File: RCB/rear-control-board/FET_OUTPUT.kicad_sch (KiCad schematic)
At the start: 3 parts, among them Q3 STB15N80K5, Q4 STB15N80K5, Q5 STB15N80K5

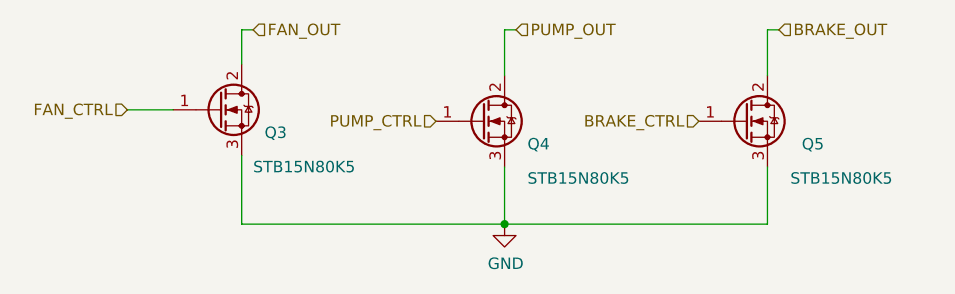
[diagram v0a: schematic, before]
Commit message: working on layout
Updating traces for RCB and organizing HVB
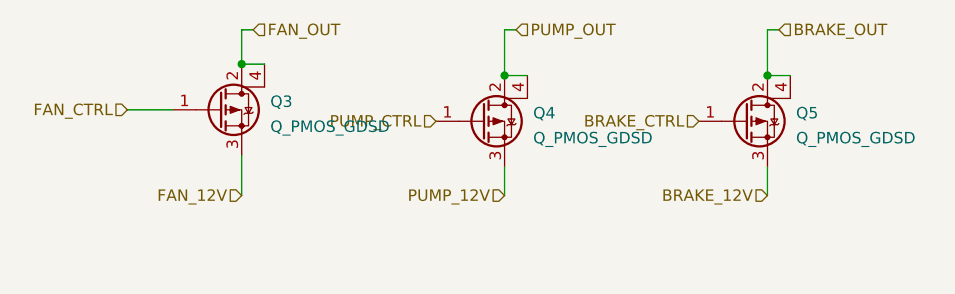
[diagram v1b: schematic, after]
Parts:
- removed Q3, Q4, Q5: STB15N80K5, Package_TO_SOT_SMD:TO-263-2, symbol Transistor_FET:STB15N80K5
- added Q3, Q4, Q5: Q_PMOS_GDSD, Package_TO_SOT_SMD:TO-252-3_TabPin4, symbol Device:Q_PMOS_GDSD
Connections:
- net BRAKE_CTRL: now also Q5.1 (G)
- net BRAKE_OUT: now also Q5.2 (D), Q5.4 (D)
- net FAN_CTRL: now also Q3.1 (G)
- net FAN_OUT: now also Q3.2 (D), Q3.4 (D)
- net PUMP_CTRL: now also Q4.1 (G)
- net PUMP_OUT: now also Q4.2 (D), Q4.4 (D)
- new net BRAKE_12V: Q5.3 (S)
- new net FAN_12V: Q3.3 (S)
- new net PUMP_12V: Q4.3 (S)
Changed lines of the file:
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@@
 (kicad_sch (version 20211123) (generator eeschema)
   (paper "A4")
-  (junction (at 87.63 81.28) (diameter 0) (color 0 0 0 0)
+  (junction (at 87.63 64.77) (diameter 0) (color 0 0 0 0)
   )
-  (wire (pts (xy 58.42 81.28) (xy 87.63 81.28))
+  (junction (at 116.84 64.77) (diameter 0) (color 0 0 0 0)
+  )
+  (junction (at 58.42 63.5) (diameter 0) (color 0 0 0 0)
+  )
+  (wire (pts (xy 87.63 64.77) (xy 90.17 64.77))
     (stroke (width 0) (type default) (color 0 0 0 0))
   )
-  (wire (pts (xy 87.63 81.28) (xy 87.63 74.93))
+  (wire (pts (xy 58.42 73.66) (xy 58.42 78.105))
     (stroke (width 0) (type default) (color 0 0 0 0))
   )
@@
     (stroke (width 0) (type default) (color 0 0 0 0))
   )
+  (wire (pts (xy 58.42 63.5) (xy 60.96 63.5))
+    (stroke (width 0) (type default) (color 0 0 0 0))
+  )
+  (wire (pts (xy 87.63 74.93) (xy 87.63 78.105))
+    (stroke (width 0) (type default) (color 0 0 0 0))
+  )
+  (wire (pts (xy 116.84 64.77) (xy 119.38 64.77))
+    (stroke (width 0) (type default) (color 0 0 0 0))
+  )
   (wire (pts (xy 87.63 59.69) (xy 87.63 64.77))
     (stroke (width 0) (type default) (color 0 0 0 0))
   )
   (wire (pts (xy 59.69 59.69) (xy 58.42 59.69))
-    (stroke (width 0) (type default) (color 0 0 0 0))
-  )
-  (wire (pts (xy 58.42 73.66) (xy 58.42 81.28))
     (stroke (width 0) (type default) (color 0 0 0 0))
   )
@@
     (stroke (width 0) (type default) (color 0 0 0 0))
   )
-  (wire (pts (xy 116.84 74.93) (xy 116.84 81.28))
+  (wire (pts (xy 45.72 68.58) (xy 50.8 68.58))
     (stroke (width 0) (type default) (color 0 0 0 0))
   )
-  (wire (pts (xy 116.84 81.28) (xy 87.63 81.28))
+  (wire (pts (xy 116.84 74.93) (xy 116.84 78.105))
     (stroke (width 0) (type default) (color 0 0 0 0))
   )
-  (wire (pts (xy 45.72 68.58) (xy 50.8 68.58))
-    (stroke (width 0) (type default) (color 0 0 0 0))
+  (hierarchical_label "FAN_12V" (shape input) (at 58.42 78.105 180)
+    (effects (font (size 1.27 1.27)) (justify right))
+  )
+  (hierarchical_label "PUMP_12V" (shape input) (at 87.63 78.105 180)
+    (effects (font (size 1.27 1.27)) (justify right))
   )
   (hierarchical_label "PUMP_CTRL" (shape input) (at 80.01 69.85 180)
@@
   )
   (hierarchical_label "FAN_CTRL" (shape input) (at 45.72 68.58 180)
+    (effects (font (size 1.27 1.27)) (justify right))
+  )
+  (hierarchical_label "BRAKE_12V" (shape input) (at 116.84 78.105 180)
     (effects (font (size 1.27 1.27)) (justify right))
   )
@@
     (effects (font (size 1.27 1.27)) (justify right))
   )
-  (symbol (lib_id "Transistor_FET:STB15N80K5") (at 55.88 68.58 0) (unit 1)
-    (in_bom yes) (on_board yes)
-    (property "Reference" "Q3" (id 0) (at 60.96 71.12 0)
+  (symbol (lib_id "Device:Q_PMOS_GDSD") (at 114.3 69.85 0) (unit 1)
+    (in_bom yes) (on_board yes) (fields_autoplaced)
+    (property "Reference" "Q5" (id 0) (at 120.015 68.9415 0)
       (effects (font (size 1.27 1.27)) (justify left))
     )
-    (property "Value" "STB15N80K5" (id 1) (at 59.69 74.93 0)
+    (property "Value" "Q_PMOS_GDSD" (id 1) (at 120.015 71.7166 0)
       (effects (font (size 1.27 1.27)) (justify left))
     )
-    (property "Footprint" "Package_TO_SOT_SMD:TO-263-2" (id 2) (at 60.96 70.485 0)
-      (effects (font (size 1.27 1.27) italic) (justify left) hide)
+    (property "Footprint" "Package_TO_SOT_SMD:TO-252-3_TabPin4" (id 2) (at 119.38 67.31 0)
+      (effects (font (size 1.27 1.27)) hide)
     )
-    (property "Datasheet" "https://www.st.com/resource/en/datasheet/stb15n80k5.pdf" (id 3) (at 55.88 68.58 0)
-      (effects (font (size 1.27 1.27)) (justify left) hide)
+    (property "Datasheet" "~" (id 3) (at 114.3 69.85 0)
+      (effects (font (size 1.27 1.27)) hide)
     )
     (pin "1")
     (pin "2")
     (pin "3")
+    (pin "4")
   )
-  (symbol (lib_id "power:GND") (at 87.63 81.28 0) (unit 1)
-    (in_bom yes) (on_board yes)
-    (property "Reference" "#PWR0121" (id 0) (at 87.63 87.63 0)
+  (symbol (lib_id "Device:Q_PMOS_GDSD") (at 85.09 69.85 0) (unit 1)
+    (in_bom yes) (on_board yes) (fields_autoplaced)
+    (property "Reference" "Q4" (id 0) (at 90.805 68.9415 0)
+      (effects (font (size 1.27 1.27)) (justify left))
+    )
+    (property "Value" "Q_PMOS_GDSD" (id 1) (at 90.805 71.7166 0)
+      (effects (font (size 1.27 1.27)) (justify left))
+    )
+    (property "Footprint" "Package_TO_SOT_SMD:TO-252-3_TabPin4" (id 2) (at 90.17 67.31 0)
       (effects (font (size 1.27 1.27)) hide)
     )
-    (property "Value" "GND" (id 1) (at 87.757 85.6742 0))
-    (property "Footprint" "" (id 2) (at 87.63 81.28 0)
+    (property "Datasheet" "~" (id 3) (at 85.09 69.85 0)
       (effects (font (size 1.27 1.27)) hide)
-    )
-    (property "Datasheet" "" (id 3) (at 87.63 81.28 0)
-      (effects (font (size 1.27 1.27)) hide)
-    )
-    (pin "1")
-  )
-  (symbol (lib_id "Transistor_FET:STB15N80K5") (at 85.09 69.85 0) (unit 1)
-    (in_bom yes) (on_board yes)
-    (property "Reference" "Q4" (id 0) (at 90.17 72.39 0)
-      (effects (font (size 1.27 1.27)) (justify left))
-    )
-    (property "Value" "STB15N80K5" (id 1) (at 90.17 76.2 0)
-      (effects (font (size 1.27 1.27)) (justify left))
-    )
-    (property "Footprint" "Package_TO_SOT_SMD:TO-263-2" (id 2) (at 90.17 71.755 0)
-      (effects (font (size 1.27 1.27) italic) (justify left) hide)
-    )
-    (property "Datasheet" "https://www.st.com/resource/en/datasheet/stb15n80k5.pdf" (id 3) (at 85.09 69.85 0)
-      (effects (font (size 1.27 1.27)) (justify left) hide)
     )
     (pin "1")
     (pin "2")
     (pin "3")
+    (pin "4")
   )
-  (symbol (lib_id "Transistor_FET:STB15N80K5") (at 114.3 69.85 0) (unit 1)
-    (in_bom yes) (on_board yes)
-    (property "Reference" "Q5" (id 0) (at 120.65 72.39 0)
+  (symbol (lib_id "Device:Q_PMOS_GDSD") (at 55.88 68.58 0) (unit 1)
+    (in_bom yes) (on_board yes) (fields_autoplaced)
+    (property "Reference" "Q3" (id 0) (at 61.595 67.6715 0)
       (effects (font (size 1.27 1.27)) (justify left))
     )
-    (property "Value" "STB15N80K5" (id 1) (at 119.38 76.2 0)
+    (property "Value" "Q_PMOS_GDSD" (id 1) (at 61.595 70.4466 0)
       (effects (font (size 1.27 1.27)) (justify left))
     )
-    (property "Footprint" "Package_TO_SOT_SMD:TO-263-2" (id 2) (at 119.38 71.755 0)
-      (effects (font (size 1.27 1.27) italic) (justify left) hide)
+    (property "Footprint" "Package_TO_SOT_SMD:TO-252-3_TabPin4" (id 2) (at 60.96 66.04 0)
+      (effects (font (size 1.27 1.27)) hide)
     )
-    (property "Datasheet" "https://www.st.com/resource/en/datasheet/stb15n80k5.pdf" (id 3) (at 114.3 69.85 0)
-      (effects (font (size 1.27 1.27)) (justify left) hide)
+    (property "Datasheet" "~" (id 3) (at 55.88 68.58 0)
+      (effects (font (size 1.27 1.27)) hide)
     )
     (pin "1")
     (pin "2")
     (pin "3")
+    (pin "4")
   )
 )

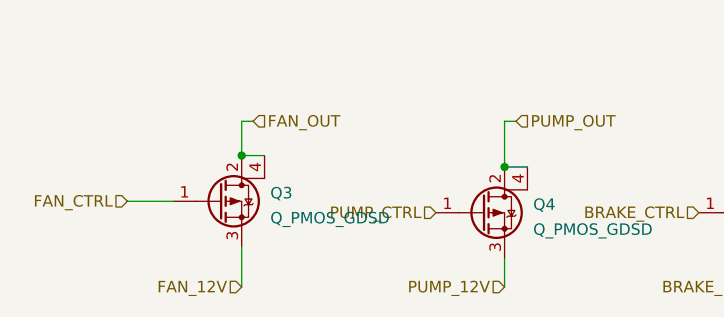
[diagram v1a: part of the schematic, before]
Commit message: updating pinouts
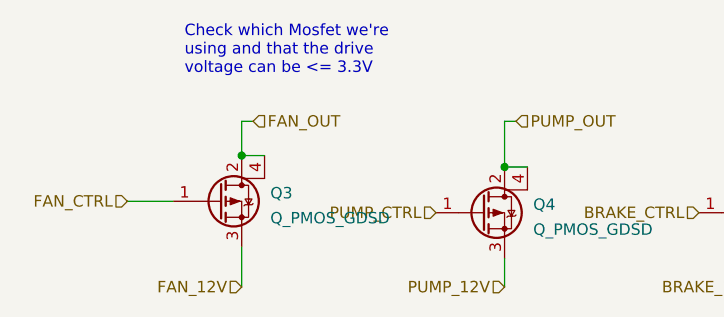
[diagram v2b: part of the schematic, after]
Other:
- note added: "Check which Mosfet we're using and that the drive voltage can be <= 3.3V"
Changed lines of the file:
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@@
     (stroke (width 0) (type default) (color 0 0 0 0))
+  )
+  (text "Check which Mosfet we're\nusing and that the drive\nvoltage can be <= 3.3V"
+    (at 52.07 54.61 0)
+    (effects (font (size 1.27 1.27)) (justify left bottom))
   )
   (hierarchical_label "FAN_12V" (shape input) (at 58.42 78.105 180)

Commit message: willem review notes
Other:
- note added: "double check how p-channels work"
- note added: "use fet that has control circuity that is n channel with high side switching. Check to make sure it works"
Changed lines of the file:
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@@
     (stroke (width 0) (type default) (color 0 0 0 0))
+  )
+  (text "double check how p-channels work" (at 29.21 82.55 0)
+    (effects (font (size 1.27 1.27)) (justify left bottom))
+  )
+  (text "use fet that has control circuity that is\nn channel with high side switching. \nCheck to make sure it works"
+    (at 67.945 90.17 0)
+    (effects (font (size 1.27 1.27)) (justify left bottom))
   )
   (text "Check which Mosfet we're\nusing and that the drive\nvoltage can be <= 3.3V"

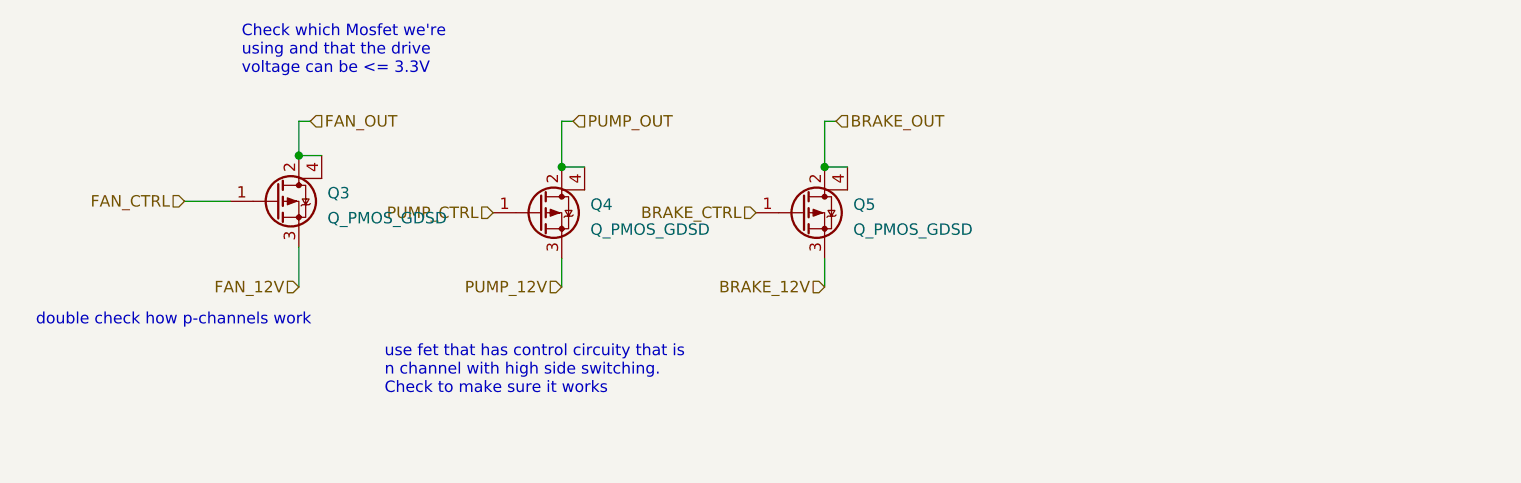
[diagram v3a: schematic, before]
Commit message: minor layout changes based on schem updates
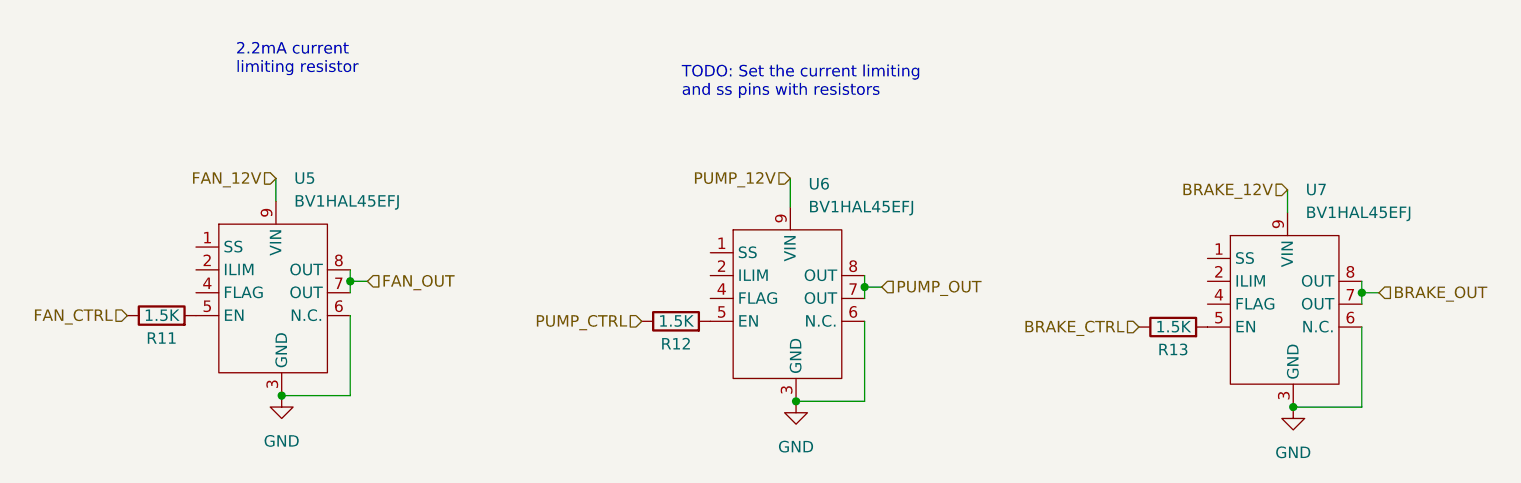
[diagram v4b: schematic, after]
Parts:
- removed Q3, Q4, Q5: Q_PMOS_GDSD, Package_TO_SOT_SMD:TO-252-3_TabPin4, symbol Device:Q_PMOS_GDSD
- added R11, R12, R13: 1.5K, Resistor_SMD:R_0603_1608Metric_Pad0.98x0.95mm_HandSolder, symbol Device:R
- added U5, U6, U7: BV1HAL45EFJ, Package_SO:HTSOP-8-1EP_3.9x4.9mm_P1.27mm_EP2.4x3.2mm_ThermalVias, symbol AERO_Symbols:BV1HAL45EFJ
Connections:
- net BRAKE_12V: now also U7.9 (VIN)
- net BRAKE_CTRL: now also R13.1
- net BRAKE_OUT: now also U7.7 (OUT), U7.8 (OUT)
- net FAN_12V: now also U5.9 (VIN)
- net FAN_CTRL: now also R11.1
- net FAN_OUT: now also U5.7 (OUT), U5.8 (OUT)
- net PUMP_12V: now also U6.9 (VIN)
- net PUMP_CTRL: now also R12.1
- net PUMP_OUT: now also U6.7 (OUT), U6.8 (OUT)
- new net: R13.2, U7.5 (EN)
- new net: R12.2, U6.5 (EN)
- new net: R11.2, U5.5 (EN)
- new net GND: U5.3 (GND), U5.6 (N.C.), U6.3 (GND), U6.6 (N.C.), U7.3 (GND), U7.6 (N.C.)
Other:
- note added: "2.2mA current limiting resistor"
- note added: "TODO: Set the current limiting and ss pins with resistors"
- note removed: "Check which Mosfet we're using and that the drive voltage can be <= 3.3V"
- note removed: "double check how p-channels work"
- note removed: "use fet that has control circuity that is n channel with high side switching. Check to make sure it works"

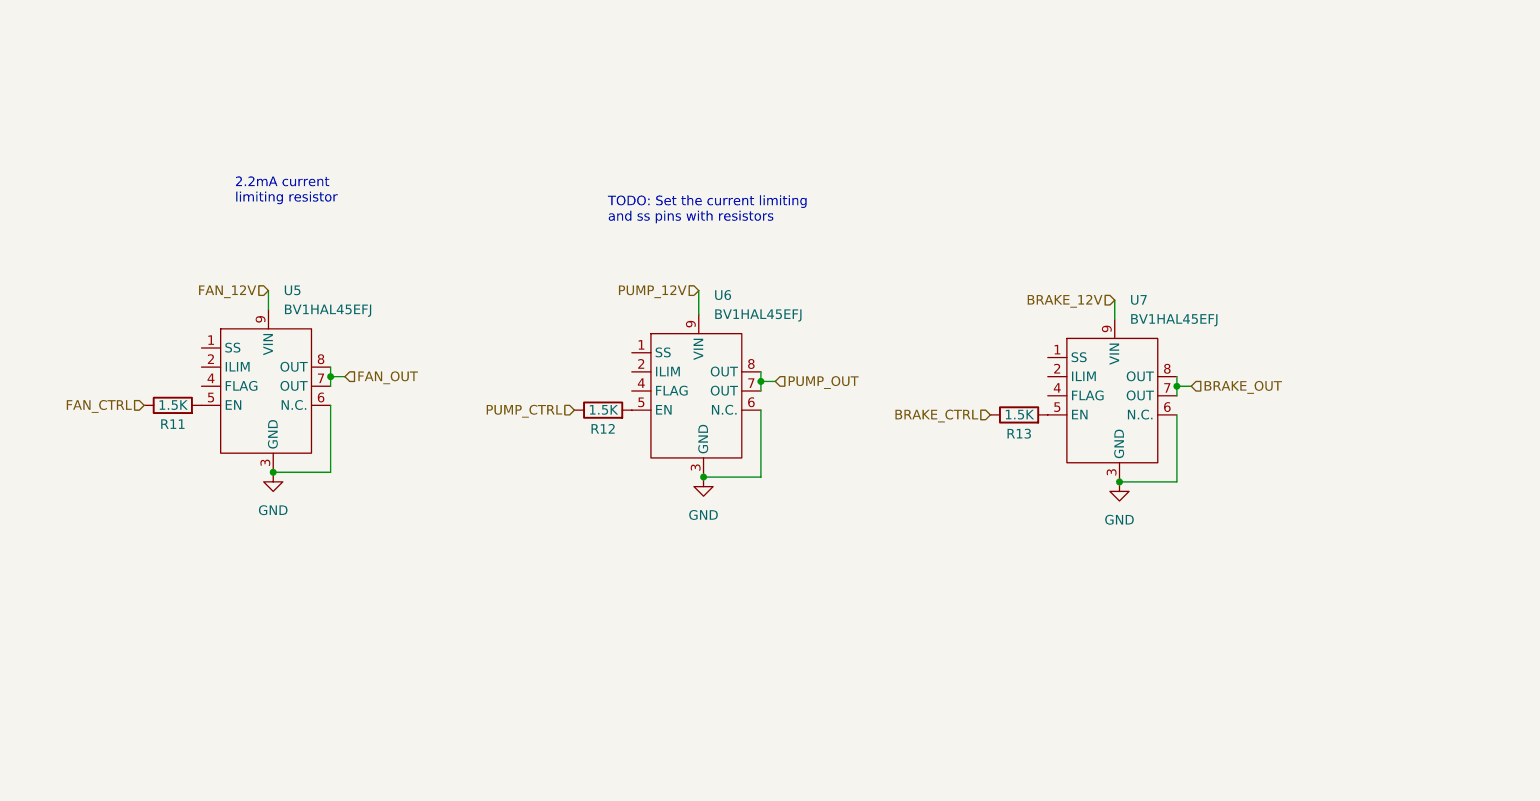
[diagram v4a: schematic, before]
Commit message: layout finished (need to place silkscreens)
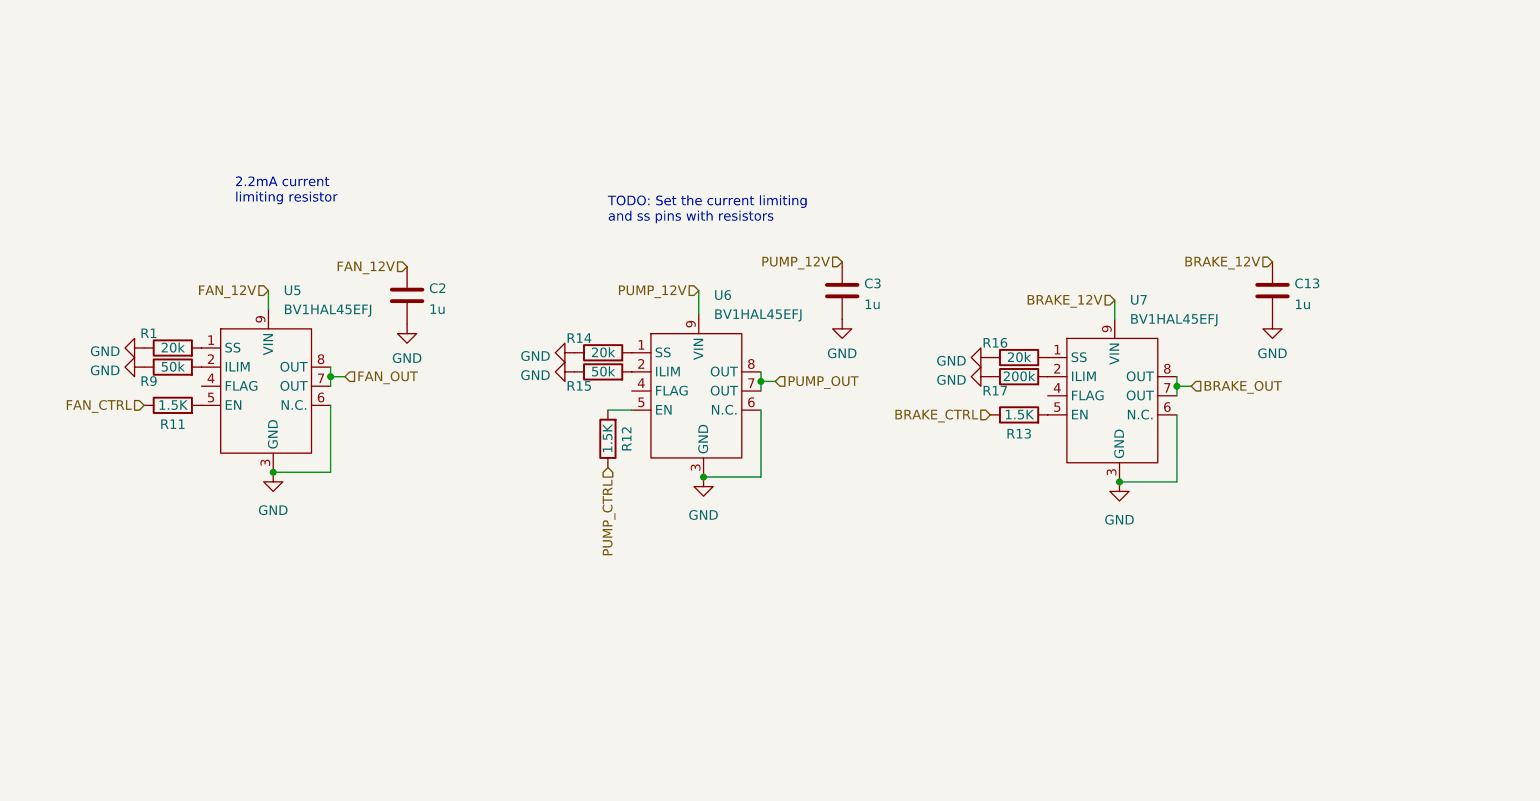
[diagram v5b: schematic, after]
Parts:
- added C13, C2, C3: 1u, Capacitor_SMD:C_0603_1608Metric_Pad1.08x0.95mm_HandSolder, symbol Device:C
- added R1, R14, R16: 20k, Resistor_SMD:R_0603_1608Metric_Pad0.98x0.95mm_HandSolder, symbol Device:R
- added R15, R9: 50k, Resistor_SMD:R_0603_1608Metric_Pad0.98x0.95mm_HandSolder, symbol Device:R
- added R17: 200k, Resistor_SMD:R_0603_1608Metric_Pad0.98x0.95mm_HandSolder, symbol Device:R
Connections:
- net BRAKE_12V: now also C13.1
- net FAN_12V: now also C2.1
- net GND: now also C13.2, C2.2, C3.2, R1.1, R14.1, R15.1, R16.1, R17.1, R9.1
- net PUMP_12V: now also C3.1
- net at U7.1 (SS): now also R16.2
- net at U7.2 (ILIM): now also R17.2
- net at U6.1 (SS): now also R14.2
- net at U6.2 (ILIM): now also R15.2
- net at U5.1 (SS): now also R1.2
- net at U5.2 (ILIM): now also R9.2
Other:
- moved on the sheet: R12

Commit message: touching up layout and making gerbers
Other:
- note removed: "TODO: Set the current limiting and ss pins with resistors"
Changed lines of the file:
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@@
     (stroke (width 0) (type default) (color 0 0 0 0))
   )
-  (text "2.2mA current \nlimiting resistor " (at 51.435 54.61 0)
+  (text "2.2mA current \nlimiting resistor " (at 45.974 60.96 0)
     (effects (font (size 1.27 1.27)) (justify left bottom))
   )
-  (text "TODO: Set the current limiting\nand ss pins with resistors"
-    (at 100.965 57.15 0)
-    (effects (font (size 1.27 1.27)) (justify left bottom))
-  )
